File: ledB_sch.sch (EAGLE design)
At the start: 6 parts, among them IC1 LM741P

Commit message: fix schema, one layer round design
and fixed the schema
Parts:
- removed IC1: LM741P, linear:LM741P
- added D1: 1N4148-2, gm-diodes:1N4148-2
- added OPAMP: LM741, linear:LM741P
- JP1: value Battery -> 6V+ GND
- JP2: value Piezo -> S+ S-
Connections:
- removed net N$3: IC1.-IN, JP2.2, R2.2
- new net N$5: D1.C, LED1.A
- new net SIG: JP2.1, OPAMP.-IN, R2.2
- net GND: now also JP2.2, OPAMP.V-; no longer IC1.V-, JP2.1, R1.1
- net N$1: now also OPAMP.+IN; no longer IC1.+IN
- net N$2: now also D1.A, OPAMP.OUT; no longer IC1.OUT, LED1.A
- net VCC: now also OPAMP.V+, R1.1; no longer IC1.V+
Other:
- note added: "ledB vcc=6v (2xCR2032)"
- moved on the sheet: JP1, JP2, LED1, R1, R2
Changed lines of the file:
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@@
 <?xml version="1.0" encoding="utf-8"?>
 <!DOCTYPE eagle SYSTEM "eagle.dtd">
-<eagle version="6.3">
+<eagle version="7.1.0">
 <drawing>
 <settings>
@@
 <setting verticaltext="up"/>
 </settings>
-<grid distance="0.1" unitdist="inch" unit="mil" style="lines" multiple="1" display="no" altdistance="0.01" altunitdist="inch" altunit="inch"/>
+<grid distance="0.1" unitdist="inch" unit="inch" style="lines" multiple="1" display="no" altdistance="0.01" altunitdist="inch" altunit="inch"/>
 <layers>
 <layer number="1" name="Top" color="4" fill="1" visible="no" active="no"/>
@@
 </classes>
 <parts>
-<part name="IC1" library="linear" deviceset="*741" device="P" technology="LM"/>
+<part name="OPAMP" library="linear" deviceset="*741" device="P" technology="LM" value="LM741"/>
 <part name="R1" library="adafruit" deviceset="R-US_" device="0207/7" value="10K"/>
 <part name="R2" library="adafruit" deviceset="R-US_" device="0207/7" value="10M"/>
 <part name="LED1" library="SparkFun-LED" deviceset="LED" device="5MM"/>
-<part name="P+1" library="SparkFun-Aesthetics" deviceset="VCC" device=""/>
-<part name="GND1" library="SparkFun-Aesthetics" deviceset="GND" device=""/>
-<part name="GND3" library="SparkFun-Aesthetics" deviceset="GND" device=""/>
 <part name="GND4" library="SparkFun-Aesthetics" deviceset="GND" device=""/>
-<part name="JP1" library="microbuilder" deviceset="HEADER-1X2" device="" value="Battery"/>
-<part name="JP2" library="microbuilder" deviceset="HEADER-1X2" device="" value="Piezo"/>
+<part name="JP1" library="microbuilder" deviceset="HEADER-1X2" device="" value="6V+     GND"/>
+<part name="JP2" library="microbuilder" deviceset="HEADER-1X2" device="" value="S+     S-"/>
 <part name="P+2" library="SparkFun-Aesthetics" deviceset="VCC" device=""/>
 <part name="GND2" library="SparkFun-Aesthetics" deviceset="GND" device=""/>
+<part name="D1" library="gm-diodes" deviceset="1N4148" device="-2"/>
+<part name="GND1" library="SparkFun-Aesthetics" deviceset="GND" device=""/>
+<part name="P+3" library="SparkFun-Aesthetics" deviceset="VCC" device=""/>
+<part name="GND3" library="SparkFun-Aesthetics" deviceset="GND" device=""/>
 </parts>
 <sheets>
 <sheet>
 <plain>
+<text x="2.54" y="0" size="1.778" layer="91">ledB
+vcc=6v (2xCR2032)</text>
 </plain>
 <instances>
-<instance part="IC1" gate="A" x="38.1" y="20.32" smashed="yes">
-<attribute name="NAME" x="30.226" y="27.305" size="1.778" layer="95"/>
-<attribute name="VALUE" x="40.64" y="15.24" size="1.778" layer="96"/>
+<instance part="OPAMP" gate="A" x="35.56" y="38.1" smashed="yes">
+<attribute name="VALUE" x="38.1" y="33.02" size="1.778" layer="96"/>
 </instance>
-<instance part="R1" gate="G$1" x="22.86" y="22.86"/>
-<instance part="R2" gate="G$1" x="48.26" y="33.02" rot="R180"/>
-<instance part="LED1" gate="G$1" x="58.42" y="20.32" rot="R90"/>
-<instance part="P+1" gate="1" x="35.56" y="38.1"/>
-<instance part="GND1" gate="1" x="10.16" y="10.16" rot="MR0"/>
-<instance part="GND3" gate="1" x="35.56" y="10.16"/>
-<instance part="GND4" gate="1" x="66.04" y="15.24"/>
-<instance part="JP1" gate="G$1" x="5.08" y="0" rot="MR180"/>
-<instance part="JP2" gate="G$1" x="0" y="33.02" rot="R180"/>
-<instance part="P+2" gate="1" x="-7.62" y="2.54"/>
-<instance part="GND2" gate="1" x="-7.62" y="-7.62"/>
+<instance part="R1" gate="G$1" x="20.32" y="40.64"/>
+<instance part="R2" gate="G$1" x="43.18" y="22.86" rot="R180"/>
+<instance part="LED1" gate="G$1" x="68.58" y="38.1" rot="R90"/>
+<instance part="GND4" gate="1" x="76.2" y="27.94"/>
+<instance part="JP1" gate="G$1" x="73.66" y="58.42" rot="MR180"/>
+<instance part="JP2" gate="G$1" x="7.62" y="33.02" smashed="yes" rot="MR0">
+<attribute name="NAME" x="8.89" y="38.735" size="1.778" layer="95" rot="MR0"/>
+<attribute name="VALUE" x="13.97" y="27.94" size="1.778" layer="96" rot="MR0"/>
+</instance>
+<instance part="P+2" gate="1" x="60.96" y="58.42"/>
+<instance part="GND2" gate="1" x="60.96" y="53.34"/>
+<instance part="D1" gate="G$1" x="58.42" y="38.1"/>
+<instance part="GND1" gate="1" x="20.32" y="30.48" rot="MR0"/>
+<instance part="P+3" gate="1" x="33.02" y="48.26"/>
+<instance part="GND3" gate="1" x="33.02" y="27.94"/>
 </instances>
 <busses>
 </busses>
 <nets>
-<net name="N$1" class="0">
-<segment>
-<pinref part="IC1" gate="A" pin="+IN"/>
-<pinref part="R1" gate="G$1" pin="2"/>
-<wire x1="27.94" y1="22.86" x2="30.48" y2="22.86" width="0.1524" layer="91"/>
-</segment>
-</net>
 <net name="GND" class="0">
 <segment>
-<pinref part="R1" gate="G$1" pin="1"/>
-<pinref part="JP2" gate="G$1" pin="1"/>
-<pinref part="GND1" gate="1" pin="GND"/>
-<wire x1="2.54" y1="30.48" x2="10.16" y2="30.48" width="0.1524" layer="91"/>
-<wire x1="10.16" y1="30.48" x2="10.16" y2="22.86" width="0.1524" layer="91"/>
-<wire x1="10.16" y1="22.86" x2="10.16" y2="12.7" width="0.1524" layer="91"/>
-<wire x1="17.78" y1="22.86" x2="10.16" y2="22.86" width="0.1524" layer="91"/>
-<junction x="10.16" y="22.86"/>
-</segment>
-<segment>
-<pinref part="IC1" gate="A" pin="V-"/>
+<pinref part="OPAMP" gate="A" pin="V-"/>
 <pinref part="GND3" gate="1" pin="GND"/>
 </segment>
@@
 <pinref part="LED1" gate="G$1" pin="C"/>
 <pinref part="GND4" gate="1" pin="GND"/>
-<wire x1="66.04" y1="17.78" x2="66.04" y2="20.32" width="0.1524" layer="91"/>
-<wire x1="66.04" y1="20.32" x2="63.5" y2="20.32" width="0.1524" layer="91"/>
+<wire x1="76.2" y1="30.48" x2="76.2" y2="38.1" width="0.1524" layer="91"/>
+<wire x1="76.2" y1="38.1" x2="73.66" y2="38.1" width="0.1524" layer="91"/>
 </segment>
 <segment>
 <pinref part="JP1" gate="G$1" pin="1"/>
 <pinref part="GND2" gate="1" pin="GND"/>
-<wire x1="2.54" y1="-2.54" x2="-7.62" y2="-2.54" width="0.1524" layer="91"/>
-<wire x1="-7.62" y1="-2.54" x2="-7.62" y2="-5.08" width="0.1524" layer="91"/>
+<wire x1="71.12" y1="55.88" x2="60.96" y2="55.88" width="0.1524" layer="91"/>
+</segment>
+<segment>
+<pinref part="GND1" gate="1" pin="GND"/>
+<pinref part="JP2" gate="G$1" pin="2"/>
+<wire x1="20.32" y1="33.02" x2="10.16" y2="33.02" width="0.1524" layer="91"/>
 </segment>
 </net>
 <net name="VCC" class="0">
-<segment>
-<pinref part="IC1" gate="A" pin="V+"/>
-<pinref part="P+1" gate="1" pin="VCC"/>
-<wire x1="35.56" y1="38.1" x2="35.56" y2="27.94" width="0.1524" layer="91"/>
-</segment>
 <segment>
 <pinref part="JP1" gate="G$1" pin="2"/>
 <pinref part="P+2" gate="1" pin="VCC"/>
-<wire x1="2.54" y1="0" x2="-7.62" y2="0" width="0.1524" layer="91"/>
-<wire x1="-7.62" y1="0" x2="-7.62" y2="2.54" width="0.1524" layer="91"/>
+<wire x1="71.12" y1="58.42" x2="60.96" y2="58.42" width="0.1524" layer="91"/>
+</segment>
+<segment>
+<pinref part="R1" gate="G$1" pin="1"/>
+<wire x1="12.7" y1="45.72" x2="12.7" y2="40.64" width="0.1524" layer="91"/>
+<wire x1="12.7" y1="40.64" x2="15.24" y2="40.64" width="0.1524" layer="91"/>
+<pinref part="OPAMP" gate="A" pin="V+"/>
+<wire x1="12.7" y1="45.72" x2="33.02" y2="45.72" width="0.1524" layer="91"/>
+<pinref part="P+3" gate="1" pin="VCC"/>
+<wire x1="33.02" y1="48.26" x2="33.02" y2="45.72" width="0.1524" layer="91"/>
+<junction x="33.02" y="45.72"/>
 </segment>
 </net>
 <net name="N$2" class="0">
 <segment>
-<pinref part="IC1" gate="A" pin="OUT"/>
 <pinref part="R2" gate="G$1" pin="1"/>
-<wire x1="53.34" y1="33.02" x2="55.88" y2="33.02" width="0.1524" layer="91"/>
-<wire x1="55.88" y1="33.02" x2="55.88" y2="20.32" width="0.1524" layer="91"/>
-<wire x1="55.88" y1="20.32" x2="45.72" y2="20.32" width="0.1524" layer="91"/>
+<pinref part="D1" gate="G$1" pin="A"/>
+<pinref part="OPAMP" gate="A" pin="OUT"/>
+<wire x1="53.34" y1="38.1" x2="50.8" y2="38.1" width="0.1524" layer="91"/>
+<wire x1="50.8" y1="38.1" x2="43.18" y2="38.1" width="0.1524" layer="91"/>
+<wire x1="48.26" y1="22.86" x2="50.8" y2="22.86" width="0.1524" layer="91"/>
+<wire x1="50.8" y1="22.86" x2="50.8" y2="38.1" width="0.1524" layer="91"/>
+<junction x="50.8" y="38.1"/>
+</segment>
+</net>
+<net name="N$5" class="0">
+<segment>
 <pinref part="LED1" gate="G$1" pin="A"/>
-<junction x="55.88" y="20.32"/>
-</segment>
-</net>
-<net name="N$3" class="0">
-<segment>
-<pinref part="IC1" gate="A" pin="-IN"/>
-<wire x1="12.7" y1="33.02" x2="12.7" y2="17.78" width="0.2032" layer="91"/>
-<wire x1="12.7" y1="17.78" x2="30.48" y2="17.78" width="0.2032" layer="91"/>
+<pinref part="D1" gate="G$1" pin="C"/>
+<wire x1="60.96" y1="38.1" x2="66.04" y2="38.1" width="0.1524" layer="91"/>
+</segment>
+</net>
+<net name="SIG" class="0">
+<segment>
+<pinref part="OPAMP" gate="A" pin="-IN"/>
+<wire x1="38.1" y1="22.86" x2="25.4" y2="22.86" width="0.2032" layer="91"/>
+<wire x1="25.4" y1="22.86" x2="25.4" y2="35.56" width="0.2032" layer="91"/>
+<wire x1="25.4" y1="35.56" x2="27.94" y2="35.56" width="0.2032" layer="91"/>
 <pinref part="R2" gate="G$1" pin="2"/>
-<wire x1="12.7" y1="33.02" x2="43.18" y2="33.02" width="0.2032" layer="91"/>
-<pinref part="JP2" gate="G$1" pin="2"/>
-<wire x1="12.7" y1="33.02" x2="2.54" y2="33.02" width="0.1524" layer="91"/>
-<junction x="12.7" y="33.02"/>
+<wire x1="10.16" y1="35.56" x2="25.4" y2="35.56" width="0.1524" layer="91"/>
+<junction x="25.4" y="35.56"/>
+<pinref part="JP2" gate="G$1" pin="1"/>
+</segment>
+</net>
+<net name="N$1" class="0">
+<segment>
+<pinref part="OPAMP" gate="A" pin="+IN"/>
+<pinref part="R1" gate="G$1" pin="2"/>
+<wire x1="25.4" y1="40.64" x2="27.94" y2="40.64" width="0.1524" layer="91"/>
 </segment>
 </net>
@@
 </schematic>
 </drawing>
+<compatibility>
+<note version="6.3" minversion="6.2.2" severity="warning">
+Since Version 6.2.2 text objects can contain more than one line,
+which will not be processed correctly with this version.
+</note>
+</compatibility>
 </eagle>

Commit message: add image and fix schema
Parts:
- removed JP2: S+ S-, microbuilder:HEADER-1X2
- added U1: PIEZO, ledB_sch:PIEZO
- OPAMP: device linear:LM741P -> ledB_sch:LM741P
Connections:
- net GND: now also R1.1, U1.GND; no longer JP2.2
- net SIG: now also U1.OUT+; no longer JP2.1
- net VCC: no longer R1.1

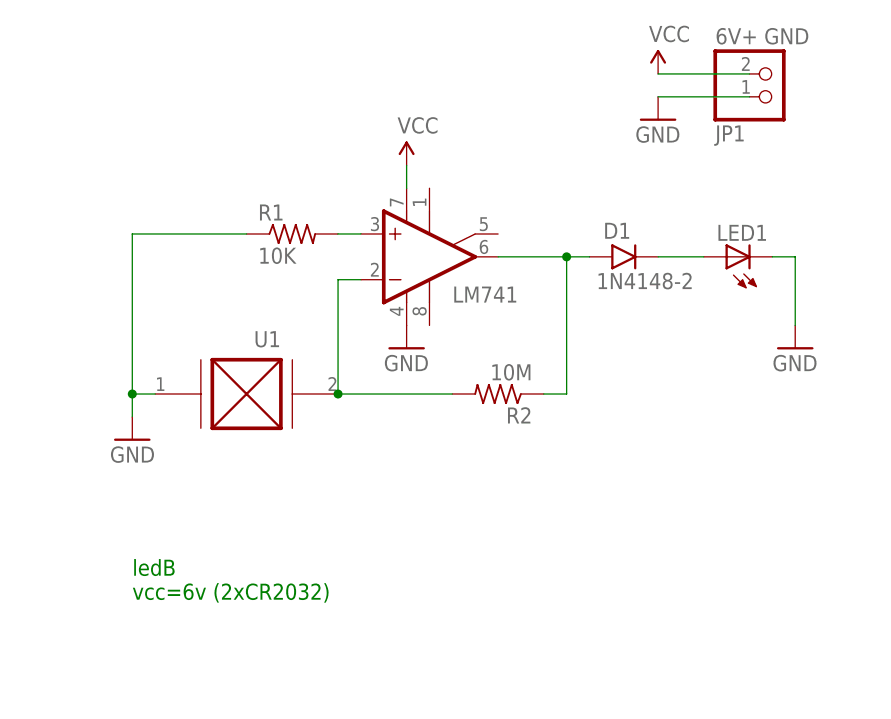
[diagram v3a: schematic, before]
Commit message: added topoR assited routing
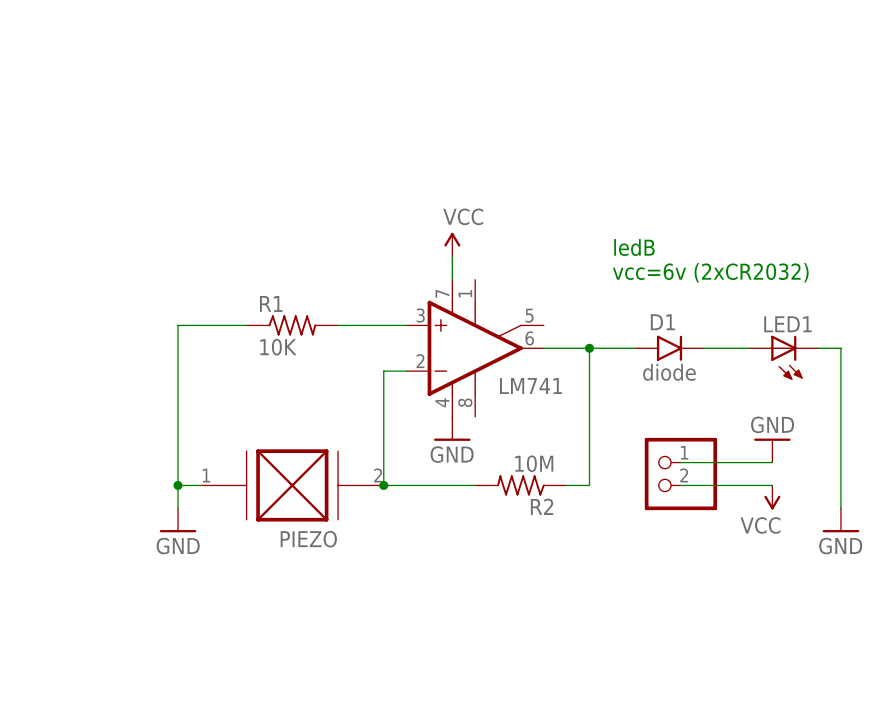
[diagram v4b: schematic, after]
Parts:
- removed U1: PIEZO, ledB_sch:PIEZO
- added PIEZO: PIEZO, ledB_sch:PIEZO
- D1: value 1N4148-2 -> diode; device gm-diodes:1N4148-2 -> ledB_sch:1N4148-3
- JP1: value 6V+ GND -> 6V+; device microbuilder:HEADER-1X2 -> ledB_sch:HEADER-1X2
- LED1: device SparkFun-LED:LED5MM -> ledB_sch:LED5MM
- R1, R2: device adafruit:R-US_0207/7 -> ledB_sch:R-US_0204/7
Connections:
- net GND: now also PIEZO.GND; no longer U1.GND
- net SIG: now also PIEZO.OUT+; no longer U1.OUT+
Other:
- moved on the sheet: D1, LED1, R1, R2
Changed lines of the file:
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@@
 <parts>
 <part name="OPAMP" library="ledB_sch" deviceset="*741" device="P" technology="LM" value="LM741"/>
-<part name="R1" library="adafruit" deviceset="R-US_" device="0207/7" value="10K"/>
-<part name="R2" library="adafruit" deviceset="R-US_" device="0207/7" value="10M"/>
-<part name="LED1" library="SparkFun-LED" deviceset="LED" device="5MM"/>
-<part name="GND4" library="SparkFun-Aesthetics" deviceset="GND" device=""/>
-<part name="JP1" library="microbuilder" deviceset="HEADER-1X2" device="" value="6V+     GND"/>
-<part name="P+2" library="SparkFun-Aesthetics" deviceset="VCC" device=""/>
-<part name="GND2" library="SparkFun-Aesthetics" deviceset="GND" device=""/>
-<part name="D1" library="gm-diodes" deviceset="1N4148" device="-2"/>
-<part name="GND1" library="SparkFun-Aesthetics" deviceset="GND" device=""/>
-<part name="P+3" library="SparkFun-Aesthetics" deviceset="VCC" device=""/>
-<part name="GND3" library="SparkFun-Aesthetics" deviceset="GND" device=""/>
-<part name="U1" library="ledB_sch" deviceset="PIEZO" device=""/>
+<part name="R1" library="ledB_sch" deviceset="R-US_" device="0204/7" value="10K"/>
+<part name="R2" library="ledB_sch" deviceset="R-US_" device="0204/7" value="10M"/>
+<part name="LED1" library="ledB_sch" deviceset="LED" device="5MM"/>
+<part name="GND4" library="ledB_sch" deviceset="GND" device=""/>
+<part name="JP1" library="ledB_sch" deviceset="HEADER-1X2" device="" value="6V+"/>
+<part name="P+2" library="ledB_sch" deviceset="VCC" device=""/>
+<part name="GND2" library="ledB_sch" deviceset="GND" device=""/>
+<part name="D1" library="ledB_sch" deviceset="1N4148" device="-3" value="diode"/>
+<part name="GND1" library="ledB_sch" deviceset="GND" device=""/>
+<part name="P+3" library="ledB_sch" deviceset="VCC" device=""/>
+<part name="GND3" library="ledB_sch" deviceset="GND" device=""/>
+<part name="PIEZO" library="ledB_sch" deviceset="PIEZO" device=""/>
 </parts>
 <sheets>
 <sheet>
 <plain>
-<text x="2.54" y="0" size="1.778" layer="91">ledB
+<text x="55.88" y="35.56" size="1.778" layer="91">ledB
 vcc=6v (2xCR2032)</text>
 </plain>
 <instances>
-<instance part="OPAMP" gate="A" x="35.56" y="38.1" smashed="yes">
-<attribute name="VALUE" x="38.1" y="33.02" size="1.778" layer="96"/>
+<instance part="OPAMP" gate="A" x="40.64" y="27.94" smashed="yes">
+<attribute name="VALUE" x="43.18" y="22.86" size="1.778" layer="96"/>
 </instance>
-<instance part="R1" gate="G$1" x="20.32" y="40.64"/>
-<instance part="R2" gate="G$1" x="43.18" y="22.86" rot="R180"/>
-<instance part="LED1" gate="G$1" x="68.58" y="38.1" rot="R90"/>
-<instance part="GND4" gate="1" x="76.2" y="27.94"/>
-<instance part="JP1" gate="G$1" x="73.66" y="58.42" rot="MR180"/>
-<instance part="P+2" gate="1" x="60.96" y="58.42"/>
-<instance part="GND2" gate="1" x="60.96" y="53.34"/>
-<instance part="D1" gate="G$1" x="58.42" y="38.1"/>
-<instance part="GND1" gate="1" x="2.54" y="17.78" rot="MR0"/>
-<instance part="P+3" gate="1" x="33.02" y="48.26"/>
-<instance part="GND3" gate="1" x="33.02" y="27.94"/>
-<instance part="U1" gate="G$1" x="15.24" y="22.86" smashed="yes" rot="R180">
-<attribute name="NAME" x="19.05" y="29.845" size="1.778" layer="95" rot="R180"/>
+<instance part="R1" gate="G$1" x="20.32" y="30.48"/>
+<instance part="R2" gate="G$1" x="45.72" y="12.7" rot="R180"/>
+<instance part="LED1" gate="G$1" x="73.66" y="27.94" rot="R90"/>
+<instance part="GND4" gate="1" x="81.28" y="7.62"/>
+<instance part="JP1" gate="G$1" x="60.96" y="12.7" smashed="yes" rot="MR0"/>
+<instance part="P+2" gate="1" x="73.66" y="12.7" rot="R180"/>
+<instance part="GND2" gate="1" x="73.66" y="17.78" rot="R180"/>
+<instance part="D1" gate="G$1" x="63.5" y="27.94"/>
+<instance part="GND1" gate="1" x="7.62" y="7.62" rot="MR0"/>
+<instance part="P+3" gate="1" x="38.1" y="38.1"/>
+<instance part="GND3" gate="1" x="38.1" y="17.78"/>
+<instance part="PIEZO" gate="G$1" x="20.32" y="12.7" smashed="yes" rot="R180">
+<attribute name="VALUE" x="25.4" y="7.62" size="1.778" layer="96" rot="R180"/>
 </instance>
 </instances>
@@
 <pinref part="LED1" gate="G$1" pin="C"/>
 <pinref part="GND4" gate="1" pin="GND"/>
-<wire x1="76.2" y1="30.48" x2="76.2" y2="38.1" width="0.1524" layer="91"/>
-<wire x1="76.2" y1="38.1" x2="73.66" y2="38.1" width="0.1524" layer="91"/>
+<wire x1="81.28" y1="10.16" x2="81.28" y2="27.94" width="0.1524" layer="91"/>
+<wire x1="81.28" y1="27.94" x2="78.74" y2="27.94" width="0.1524" layer="91"/>
 </segment>
 <segment>
 <pinref part="JP1" gate="G$1" pin="1"/>
 <pinref part="GND2" gate="1" pin="GND"/>
-<wire x1="71.12" y1="55.88" x2="60.96" y2="55.88" width="0.1524" layer="91"/>
+<wire x1="63.5" y1="15.24" x2="73.66" y2="15.24" width="0.1524" layer="91"/>
 </segment>
 <segment>
 <pinref part="GND1" gate="1" pin="GND"/>
-<pinref part="U1" gate="G$1" pin="GND"/>
-<wire x1="2.54" y1="20.32" x2="2.54" y2="22.86" width="0.1524" layer="91"/>
-<wire x1="2.54" y1="22.86" x2="5.08" y2="22.86" width="0.1524" layer="91"/>
+<pinref part="PIEZO" gate="G$1" pin="GND"/>
+<wire x1="7.62" y1="10.16" x2="7.62" y2="12.7" width="0.1524" layer="91"/>
+<wire x1="7.62" y1="12.7" x2="10.16" y2="12.7" width="0.1524" layer="91"/>
 <pinref part="R1" gate="G$1" pin="1"/>
-<wire x1="2.54" y1="40.64" x2="15.24" y2="40.64" width="0.1524" layer="91"/>
-<wire x1="2.54" y1="40.64" x2="2.54" y2="22.86" width="0.1524" layer="91"/>
-<junction x="2.54" y="22.86"/>
+<wire x1="7.62" y1="30.48" x2="15.24" y2="30.48" width="0.1524" layer="91"/>
+<wire x1="7.62" y1="30.48" x2="7.62" y2="12.7" width="0.1524" layer="91"/>
+<junction x="7.62" y="12.7"/>
 </segment>
 </net>
@@
 <pinref part="JP1" gate="G$1" pin="2"/>
 <pinref part="P+2" gate="1" pin="VCC"/>
-<wire x1="71.12" y1="58.42" x2="60.96" y2="58.42" width="0.1524" layer="91"/>
+<wire x1="63.5" y1="12.7" x2="73.66" y2="12.7" width="0.1524" layer="91"/>
 </segment>
 <segment>
 <pinref part="OPAMP" gate="A" pin="V+"/>
 <pinref part="P+3" gate="1" pin="VCC"/>
-<wire x1="33.02" y1="48.26" x2="33.02" y2="45.72" width="0.1524" layer="91"/>
+<wire x1="38.1" y1="38.1" x2="38.1" y2="35.56" width="0.1524" layer="91"/>
 </segment>
 </net>
@@
 <pinref part="D1" gate="G$1" pin="A"/>
 <pinref part="OPAMP" gate="A" pin="OUT"/>
-<wire x1="53.34" y1="38.1" x2="50.8" y2="38.1" width="0.1524" layer="91"/>
-<wire x1="50.8" y1="38.1" x2="43.18" y2="38.1" width="0.1524" layer="91"/>
-<wire x1="48.26" y1="22.86" x2="50.8" y2="22.86" width="0.1524" layer="91"/>
-<wire x1="50.8" y1="22.86" x2="50.8" y2="38.1" width="0.1524" layer="91"/>
-<junction x="50.8" y="38.1"/>
+<wire x1="58.42" y1="27.94" x2="53.34" y2="27.94" width="0.1524" layer="91"/>
+<wire x1="53.34" y1="27.94" x2="48.26" y2="27.94" width="0.1524" layer="91"/>
+<wire x1="50.8" y1="12.7" x2="53.34" y2="12.7" width="0.1524" layer="91"/>
+<wire x1="53.34" y1="12.7" x2="53.34" y2="27.94" width="0.1524" layer="91"/>
+<junction x="53.34" y="27.94"/>
 </segment>
 </net>
@@
 <pinref part="LED1" gate="G$1" pin="A"/>
 <pinref part="D1" gate="G$1" pin="C"/>
-<wire x1="60.96" y1="38.1" x2="66.04" y2="38.1" width="0.1524" layer="91"/>
+<wire x1="66.04" y1="27.94" x2="71.12" y2="27.94" width="0.1524" layer="91"/>
 </segment>
 </net>
 <net name="SIG" class="0">
 <segment>
-<wire x1="38.1" y1="22.86" x2="25.4" y2="22.86" width="0.2032" layer="91"/>
+<wire x1="40.64" y1="12.7" x2="30.48" y2="12.7" width="0.2032" layer="91"/>
 <pinref part="R2" gate="G$1" pin="2"/>
-<pinref part="U1" gate="G$1" pin="OUT+"/>
+<pinref part="PIEZO" gate="G$1" pin="OUT+"/>
 <pinref part="OPAMP" gate="A" pin="-IN"/>
-<wire x1="25.4" y1="35.56" x2="27.94" y2="35.56" width="0.2032" layer="91"/>
-<wire x1="25.4" y1="35.56" x2="25.4" y2="22.86" width="0.1524" layer="91"/>
-<junction x="25.4" y="22.86"/>
+<wire x1="30.48" y1="25.4" x2="33.02" y2="25.4" width="0.2032" layer="91"/>
+<wire x1="30.48" y1="25.4" x2="30.48" y2="12.7" width="0.1524" layer="91"/>
+<junction x="30.48" y="12.7"/>
 </segment>
 </net>
@@
 <pinref part="OPAMP" gate="A" pin="+IN"/>
 <pinref part="R1" gate="G$1" pin="2"/>
-<wire x1="25.4" y1="40.64" x2="27.94" y2="40.64" width="0.1524" layer="91"/>
+<wire x1="25.4" y1="30.48" x2="33.02" y2="30.48" width="0.1524" layer="91"/>
 </segment>
 </net>
